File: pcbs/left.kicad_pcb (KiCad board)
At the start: 2 copper layers, 121.1 x 91.2 mm, 27 parts

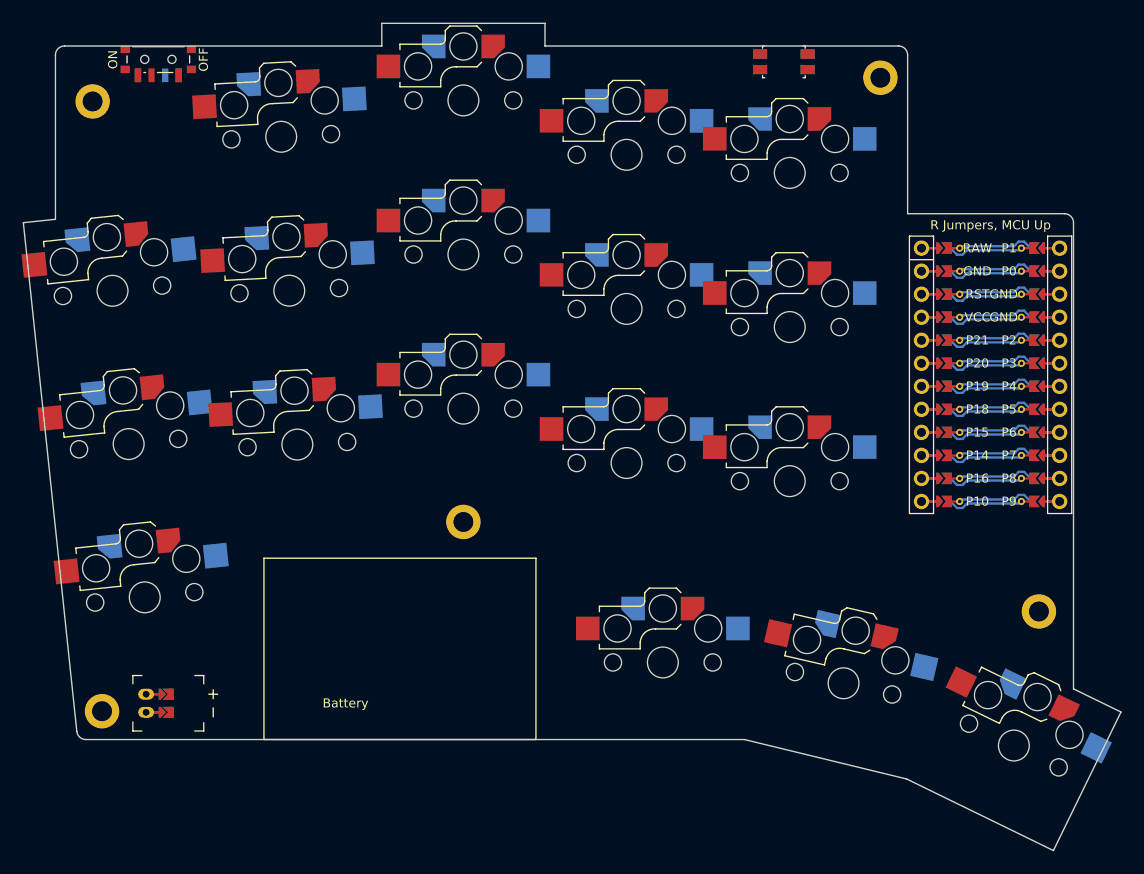
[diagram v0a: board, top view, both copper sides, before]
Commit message: Add 0.5mm between switch footprint and edge
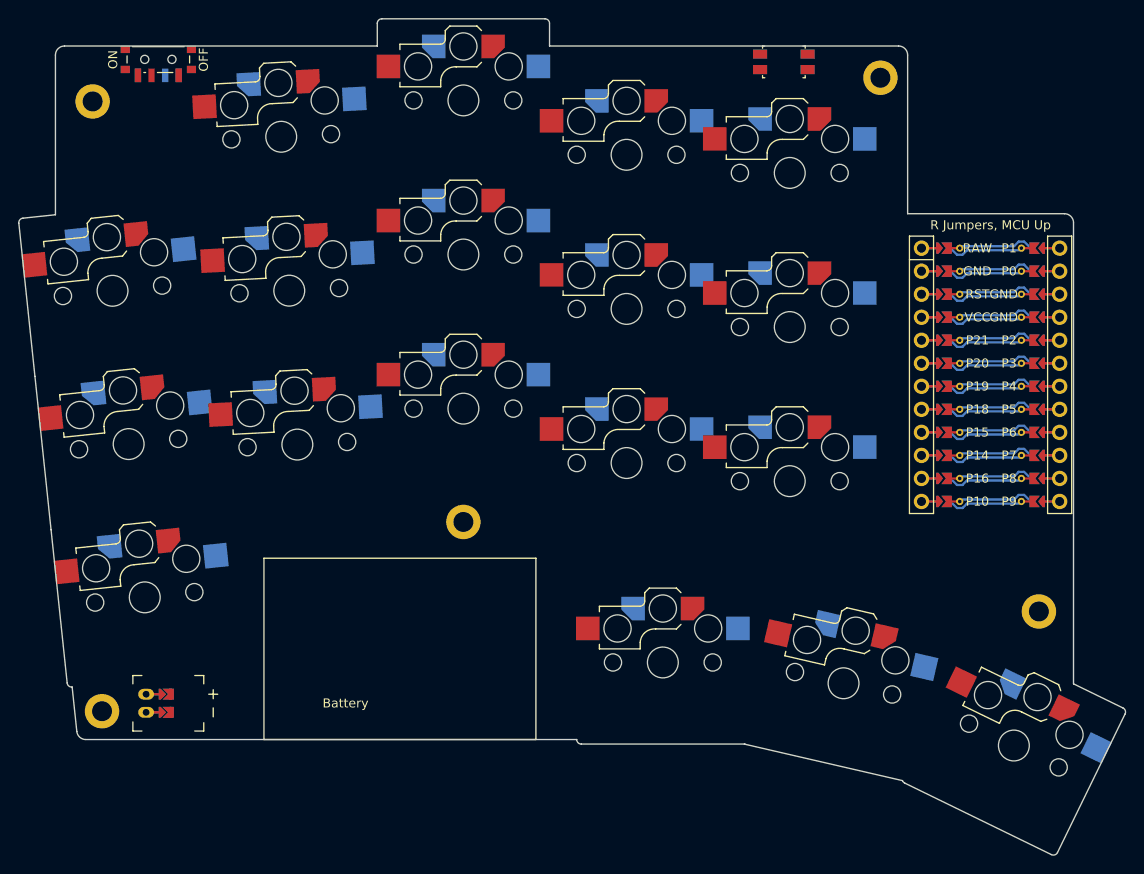
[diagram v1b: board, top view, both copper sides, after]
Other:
- board size 121.1 x 91.2 mm -> 122.1 x 92.2 mm
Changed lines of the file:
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@@
     (fp_circle (center 0 0) (end -2.1500000000000004 0) (layer "B.CrtYd") (stroke (width 0.05) (type solid)) (fill none))
   )
-  (gr_line (start 86.60684319999999 58.67357570000001) (end 92.50479308505149 114.78881969999998) (layer Edge.Cuts) (stroke (width 0.15) (type default)))
-(gr_line (start 86.60684319999999 58.67357570000001) (end 90.1483667 58.30134658019551) (layer Edge.Cuts) (stroke (width 0.15) (type default)))
-(gr_line (start 144.1483666 39.18429119999999) (end 144.1483667 36.68429119999999) (layer Edge.Cuts) (stroke (width 0.15) (type default)))
-(gr_line (start 144.1483667 36.68429119999999) (end 126.1483667 36.68429119999999) (layer Edge.Cuts) (stroke (width 0.15) (type default)))
-(gr_line (start 126.1483667 36.68429119999999) (end 126.1483667 39.18429119999999) (layer Edge.Cuts) (stroke (width 0.15) (type default)))
-(gr_line (start 93.49931498505148 115.68429119999999) (end 166.1483666 115.68429119999999) (layer Edge.Cuts) (stroke (width 0.15) (type default)))
-(gr_line (start 184.0527886 120.0396531) (end 200.23108150000002 127.93033369999999) (layer Edge.Cuts) (stroke (width 0.15) (type default)))
-(gr_line (start 200.23108150000002 127.93033369999999) (end 207.683391 112.65083489999999) (layer Edge.Cuts) (stroke (width 0.15) (type default)))
-(gr_line (start 207.683391 112.65083489999999) (end 202.4483666 110.09754292235218) (layer Edge.Cuts) (stroke (width 0.15) (type default)))
-(gr_line (start 184.0527886 120.0396531) (end 166.1483666 115.68429119999999) (layer Edge.Cuts) (stroke (width 0.15) (type default)))
+  (gr_line (start 144.6483666 39.18429119999999) (end 144.6483667 36.68429119999999) (layer Edge.Cuts) (stroke (width 0.15) (type default)))
+(gr_arc (start 144.6483667 36.68429119999999) (mid 144.5019201 36.33073779999999) (end 144.1483667 36.18429119999999) (layer Edge.Cuts) (stroke (width 0.15) (type default)))
+(gr_line (start 144.1483667 36.18429119999999) (end 126.1483667 36.18429119999999) (layer Edge.Cuts) (stroke (width 0.15) (type default)))
+(gr_arc (start 126.1483667 36.18429119999999) (mid 125.7948133 36.33073779999999) (end 125.6483667 36.68429119999999) (layer Edge.Cuts) (stroke (width 0.15) (type default)))
+(gr_line (start 125.6483667 36.68429119999999) (end 125.6483667 39.18429119999999) (layer Edge.Cuts) (stroke (width 0.15) (type default)))
+(gr_line (start 90.1483667 57.79859253261282) (end 86.55489349999999 58.176281800000005) (layer Edge.Cuts) (stroke (width 0.15) (type default)))
+(gr_arc (start 86.55457899999999 58.17631480000001) (mid 86.21827029999999 58.35891550000001) (end 86.10958229999999 58.72583990000001) (layer Edge.Cuts) (stroke (width 0.15) (type default)))
+(gr_line (start 86.10961539999998 58.726154400000006) (end 87.88653319999999 75.63239759999999) (layer Edge.Cuts) (stroke (width 0.15) (type default)))
+(gr_line (start 87.88659929999999 75.63302660000001) (end 89.66351709999999 92.5392698) (layer Edge.Cuts) (stroke (width 0.15) (type default)))
+(gr_line (start 89.66358319999999 92.53989879999999) (end 91.440501 109.446142) (layer Edge.Cuts) (stroke (width 0.15) (type default)))
+(gr_arc (start 91.4405339 109.4464565) (mid 91.6231347 109.7827653) (end 91.9900591 109.8914533) (layer Edge.Cuts) (stroke (width 0.15) (type default)))
+(gr_line (start 148.1483666 116.18429119999999) (end 166.1483666 116.18429119999999) (layer Edge.Cuts) (stroke (width 0.15) (type default)))
+(gr_arc (start 166.1483666 116.18429119999999) (mid 166.1632215 116.18407049999999) (end 166.1780633 116.18340849999998) (layer Edge.Cuts) (stroke (width 0.15) (type default)))
+(gr_arc (start 166.17806330000002 116.18340849999998) (mid 166.2319032 116.20633339999999) (end 166.28805290000003 116.22281089999998) (layer Edge.Cuts) (stroke (width 0.15) (type default)))
+(gr_line (start 166.28805290000003 116.22281089999998) (end 183.58496340000002 120.2161173) (layer Edge.Cuts) (stroke (width 0.15) (type default)))
+(gr_arc (start 183.58496340000002 120.2161173) (mid 183.68316850000002 120.376374) (end 183.833603 120.4890502) (layer Edge.Cuts) (stroke (width 0.15) (type default)))
+(gr_line (start 183.833603 120.4890501) (end 200.0118959 128.37973069999998) (layer Edge.Cuts) (stroke (width 0.15) (type default)))
+(gr_arc (start 200.0118959 128.37973069999998) (mid 200.3938655 128.40309299999998) (end 200.68047850000002 128.14951929999998) (layer Edge.Cuts) (stroke (width 0.15) (type default)))
+(gr_line (start 200.68047850000002 128.14951929999998) (end 208.132788 112.8700205) (layer Edge.Cuts) (stroke (width 0.15) (type default)))
+(gr_arc (start 208.13278800000003 112.8700205) (mid 208.15615030000004 112.48805089999999) (end 207.90257660000003 112.20143789999999) (layer Edge.Cuts) (stroke (width 0.15) (type default)))
+(gr_line (start 207.9025766 112.20143789999999) (end 202.4483666 109.54124196329977) (layer Edge.Cuts) (stroke (width 0.15) (type default)))
+(gr_arc (start 147.6483666 115.68429119999999) (mid 147.7948132 116.03784459999999) (end 148.1483666 116.18429119999999) (layer Edge.Cuts) (stroke (width 0.15) (type default)))
 (gr_line (start 184.1483667 57.684291099999996) (end 201.4483666 57.684291099999996) (layer Edge.Cuts) (stroke (width 0.15) (type default)))
-(gr_line (start 202.4483666 110.09754292235218) (end 202.4483666 58.684291099999996) (layer Edge.Cuts) (stroke (width 0.15) (type default)))
+(gr_line (start 202.4483666 109.54124196329977) (end 202.4483666 58.684291099999996) (layer Edge.Cuts) (stroke (width 0.15) (type default)))
 (gr_arc (start 202.4483666 58.684291099999996) (mid 202.1554734 57.9771843) (end 201.4483666 57.684291099999996) (layer Edge.Cuts) (stroke (width 0.15) (type default)))
+(gr_line (start 92.50479308505149 114.78881969999998) (end 91.9900591 109.8914532) (layer Edge.Cuts) (stroke (width 0.15) (type default)))
+(gr_line (start 147.6483666 115.68429119999999) (end 93.49931498505148 115.68429119999996) (layer Edge.Cuts) (stroke (width 0.15) (type default)))
 (gr_arc (start 92.50479308505149 114.78881969999996) (mid 92.83018438505148 115.42743599999996) (end 93.49931498505148 115.68429119999996) (layer Edge.Cuts) (stroke (width 0.15) (type default)))
-(gr_line (start 90.1483667 58.30134658019551) (end 90.1483667 40.18429119999999) (layer Edge.Cuts) (stroke (width 0.15) (type default)))
-(gr_line (start 91.1483667 39.18429119999999) (end 126.1483667 39.18429119999999) (layer Edge.Cuts) (stroke (width 0.15) (type default)))
-(gr_line (start 144.1483666 39.18429119999999) (end 183.1483667 39.18429119999999) (layer Edge.Cuts) (stroke (width 0.15) (type default)))
+(gr_line (start 90.1483667 57.79859253261282) (end 90.1483667 40.18429119999999) (layer Edge.Cuts) (stroke (width 0.15) (type default)))
+(gr_line (start 91.1483667 39.18429119999999) (end 125.6483667 39.18429119999999) (layer Edge.Cuts) (stroke (width 0.15) (type default)))
+(gr_line (start 144.6483666 39.18429119999999) (end 183.1483667 39.18429119999999) (layer Edge.Cuts) (stroke (width 0.15) (type default)))
 (gr_line (start 184.1483667 40.18429119999999) (end 184.1483667 57.684291099999996) (layer Edge.Cuts) (stroke (width 0.15) (type default)))
 (gr_arc (start 91.1483667 39.18429119999999) (mid 90.44125989999999 39.47718439999999) (end 90.1483667 40.18429119999999) (layer Edge.Cuts) (stroke (width 0.15) (type default)))

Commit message: Undo last change and add 1mm around controller
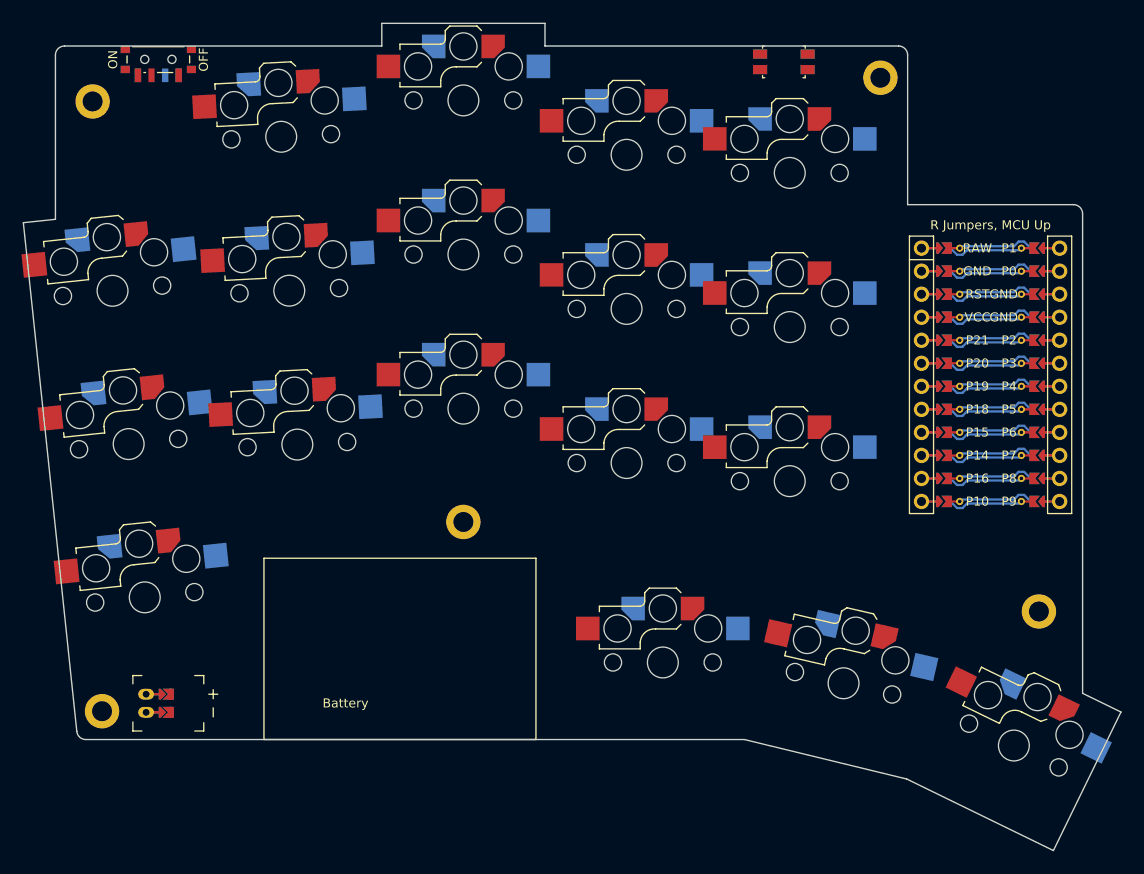
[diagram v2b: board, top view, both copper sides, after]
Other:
- board size 122.1 x 92.2 mm -> 121.1 x 91.2 mm
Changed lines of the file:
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@@
     (fp_circle (center 0 0) (end -2.1500000000000004 0) (layer "B.CrtYd") (stroke (width 0.05) (type solid)) (fill none))
   )
-  (gr_line (start 144.6483666 39.18429119999999) (end 144.6483667 36.68429119999999) (layer Edge.Cuts) (stroke (width 0.15) (type default)))
-(gr_arc (start 144.6483667 36.68429119999999) (mid 144.5019201 36.33073779999999) (end 144.1483667 36.18429119999999) (layer Edge.Cuts) (stroke (width 0.15) (type default)))
-(gr_line (start 144.1483667 36.18429119999999) (end 126.1483667 36.18429119999999) (layer Edge.Cuts) (stroke (width 0.15) (type default)))
-(gr_arc (start 126.1483667 36.18429119999999) (mid 125.7948133 36.33073779999999) (end 125.6483667 36.68429119999999) (layer Edge.Cuts) (stroke (width 0.15) (type default)))
-(gr_line (start 125.6483667 36.68429119999999) (end 125.6483667 39.18429119999999) (layer Edge.Cuts) (stroke (width 0.15) (type default)))
-(gr_line (start 90.1483667 57.79859253261282) (end 86.55489349999999 58.176281800000005) (layer Edge.Cuts) (stroke (width 0.15) (type default)))
-(gr_arc (start 86.55457899999999 58.17631480000001) (mid 86.21827029999999 58.35891550000001) (end 86.10958229999999 58.72583990000001) (layer Edge.Cuts) (stroke (width 0.15) (type default)))
-(gr_line (start 86.10961539999998 58.726154400000006) (end 87.88653319999999 75.63239759999999) (layer Edge.Cuts) (stroke (width 0.15) (type default)))
-(gr_line (start 87.88659929999999 75.63302660000001) (end 89.66351709999999 92.5392698) (layer Edge.Cuts) (stroke (width 0.15) (type default)))
-(gr_line (start 89.66358319999999 92.53989879999999) (end 91.440501 109.446142) (layer Edge.Cuts) (stroke (width 0.15) (type default)))
-(gr_arc (start 91.4405339 109.4464565) (mid 91.6231347 109.7827653) (end 91.9900591 109.8914533) (layer Edge.Cuts) (stroke (width 0.15) (type default)))
-(gr_line (start 148.1483666 116.18429119999999) (end 166.1483666 116.18429119999999) (layer Edge.Cuts) (stroke (width 0.15) (type default)))
-(gr_arc (start 166.1483666 116.18429119999999) (mid 166.1632215 116.18407049999999) (end 166.1780633 116.18340849999998) (layer Edge.Cuts) (stroke (width 0.15) (type default)))
-(gr_arc (start 166.17806330000002 116.18340849999998) (mid 166.2319032 116.20633339999999) (end 166.28805290000003 116.22281089999998) (layer Edge.Cuts) (stroke (width 0.15) (type default)))
-(gr_line (start 166.28805290000003 116.22281089999998) (end 183.58496340000002 120.2161173) (layer Edge.Cuts) (stroke (width 0.15) (type default)))
-(gr_arc (start 183.58496340000002 120.2161173) (mid 183.68316850000002 120.376374) (end 183.833603 120.4890502) (layer Edge.Cuts) (stroke (width 0.15) (type default)))
-(gr_line (start 183.833603 120.4890501) (end 200.0118959 128.37973069999998) (layer Edge.Cuts) (stroke (width 0.15) (type default)))
-(gr_arc (start 200.0118959 128.37973069999998) (mid 200.3938655 128.40309299999998) (end 200.68047850000002 128.14951929999998) (layer Edge.Cuts) (stroke (width 0.15) (type default)))
-(gr_line (start 200.68047850000002 128.14951929999998) (end 208.132788 112.8700205) (layer Edge.Cuts) (stroke (width 0.15) (type default)))
-(gr_arc (start 208.13278800000003 112.8700205) (mid 208.15615030000004 112.48805089999999) (end 207.90257660000003 112.20143789999999) (layer Edge.Cuts) (stroke (width 0.15) (type default)))
-(gr_line (start 207.9025766 112.20143789999999) (end 202.4483666 109.54124196329977) (layer Edge.Cuts) (stroke (width 0.15) (type default)))
-(gr_arc (start 147.6483666 115.68429119999999) (mid 147.7948132 116.03784459999999) (end 148.1483666 116.18429119999999) (layer Edge.Cuts) (stroke (width 0.15) (type default)))
-(gr_line (start 184.1483667 57.684291099999996) (end 201.4483666 57.684291099999996) (layer Edge.Cuts) (stroke (width 0.15) (type default)))
-(gr_line (start 202.4483666 109.54124196329977) (end 202.4483666 58.684291099999996) (layer Edge.Cuts) (stroke (width 0.15) (type default)))
-(gr_arc (start 202.4483666 58.684291099999996) (mid 202.1554734 57.9771843) (end 201.4483666 57.684291099999996) (layer Edge.Cuts) (stroke (width 0.15) (type default)))
-(gr_line (start 92.50479308505149 114.78881969999998) (end 91.9900591 109.8914532) (layer Edge.Cuts) (stroke (width 0.15) (type default)))
-(gr_line (start 147.6483666 115.68429119999999) (end 93.49931498505148 115.68429119999996) (layer Edge.Cuts) (stroke (width 0.15) (type default)))
+  (gr_line (start 86.60684319999999 58.67357570000001) (end 92.50479308505149 114.78881969999998) (layer Edge.Cuts) (stroke (width 0.15) (type default)))
+(gr_line (start 86.60684319999999 58.67357570000001) (end 90.1483667 58.30134658019551) (layer Edge.Cuts) (stroke (width 0.15) (type default)))
+(gr_line (start 144.1483666 39.18429119999999) (end 144.1483667 36.68429119999999) (layer Edge.Cuts) (stroke (width 0.15) (type default)))
+(gr_line (start 144.1483667 36.68429119999999) (end 126.1483667 36.68429119999999) (layer Edge.Cuts) (stroke (width 0.15) (type default)))
+(gr_line (start 126.1483667 36.68429119999999) (end 126.1483667 39.18429119999999) (layer Edge.Cuts) (stroke (width 0.15) (type default)))
+(gr_line (start 93.49931498505148 115.68429119999999) (end 166.1483666 115.68429119999999) (layer Edge.Cuts) (stroke (width 0.15) (type default)))
+(gr_line (start 184.0527886 120.0396531) (end 200.23108150000002 127.93033369999999) (layer Edge.Cuts) (stroke (width 0.15) (type default)))
+(gr_line (start 200.23108150000002 127.93033369999999) (end 207.683391 112.65083489999999) (layer Edge.Cuts) (stroke (width 0.15) (type default)))
+(gr_line (start 207.683391 112.65083489999999) (end 203.4483666 110.58527550630113) (layer Edge.Cuts) (stroke (width 0.15) (type default)))
+(gr_line (start 184.0527886 120.0396531) (end 166.1483666 115.68429119999999) (layer Edge.Cuts) (stroke (width 0.15) (type default)))
+(gr_line (start 184.1483667 56.684291099999996) (end 202.4483666 56.684291099999996) (layer Edge.Cuts) (stroke (width 0.15) (type default)))
+(gr_arc (start 203.4483666 57.684291099999996) (mid 203.1554734 56.9771843) (end 202.4483666 56.684291099999996) (layer Edge.Cuts) (stroke (width 0.15) (type default)))
+(gr_line (start 203.4483666 57.684291099999996) (end 203.4483666 110.58527550630113) (layer Edge.Cuts) (stroke (width 0.15) (type default)))
 (gr_arc (start 92.50479308505149 114.78881969999996) (mid 92.83018438505148 115.42743599999996) (end 93.49931498505148 115.68429119999996) (layer Edge.Cuts) (stroke (width 0.15) (type default)))
-(gr_line (start 90.1483667 57.79859253261282) (end 90.1483667 40.18429119999999) (layer Edge.Cuts) (stroke (width 0.15) (type default)))
-(gr_line (start 91.1483667 39.18429119999999) (end 125.6483667 39.18429119999999) (layer Edge.Cuts) (stroke (width 0.15) (type default)))
-(gr_line (start 144.6483666 39.18429119999999) (end 183.1483667 39.18429119999999) (layer Edge.Cuts) (stroke (width 0.15) (type default)))
-(gr_line (start 184.1483667 40.18429119999999) (end 184.1483667 57.684291099999996) (layer Edge.Cuts) (stroke (width 0.15) (type default)))
+(gr_line (start 90.1483667 58.30134658019551) (end 90.1483667 40.18429119999999) (layer Edge.Cuts) (stroke (width 0.15) (type default)))
+(gr_line (start 91.1483667 39.18429119999999) (end 126.1483667 39.18429119999999) (layer Edge.Cuts) (stroke (width 0.15) (type default)))
+(gr_line (start 144.1483666 39.18429119999999) (end 183.1483667 39.18429119999999) (layer Edge.Cuts) (stroke (width 0.15) (type default)))
+(gr_line (start 184.1483667 40.18429119999999) (end 184.1483667 56.684291099999996) (layer Edge.Cuts) (stroke (width 0.15) (type default)))
 (gr_arc (start 91.1483667 39.18429119999999) (mid 90.44125989999999 39.47718439999999) (end 90.1483667 40.18429119999999) (layer Edge.Cuts) (stroke (width 0.15) (type default)))
 (gr_arc (start 184.1483667 40.18429119999999) (mid 183.8554735 39.47718439999999) (end 183.1483667 39.18429119999999) (layer Edge.Cuts) (stroke (width 0.15) (type default)))
